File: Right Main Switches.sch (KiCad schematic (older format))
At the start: 96 parts

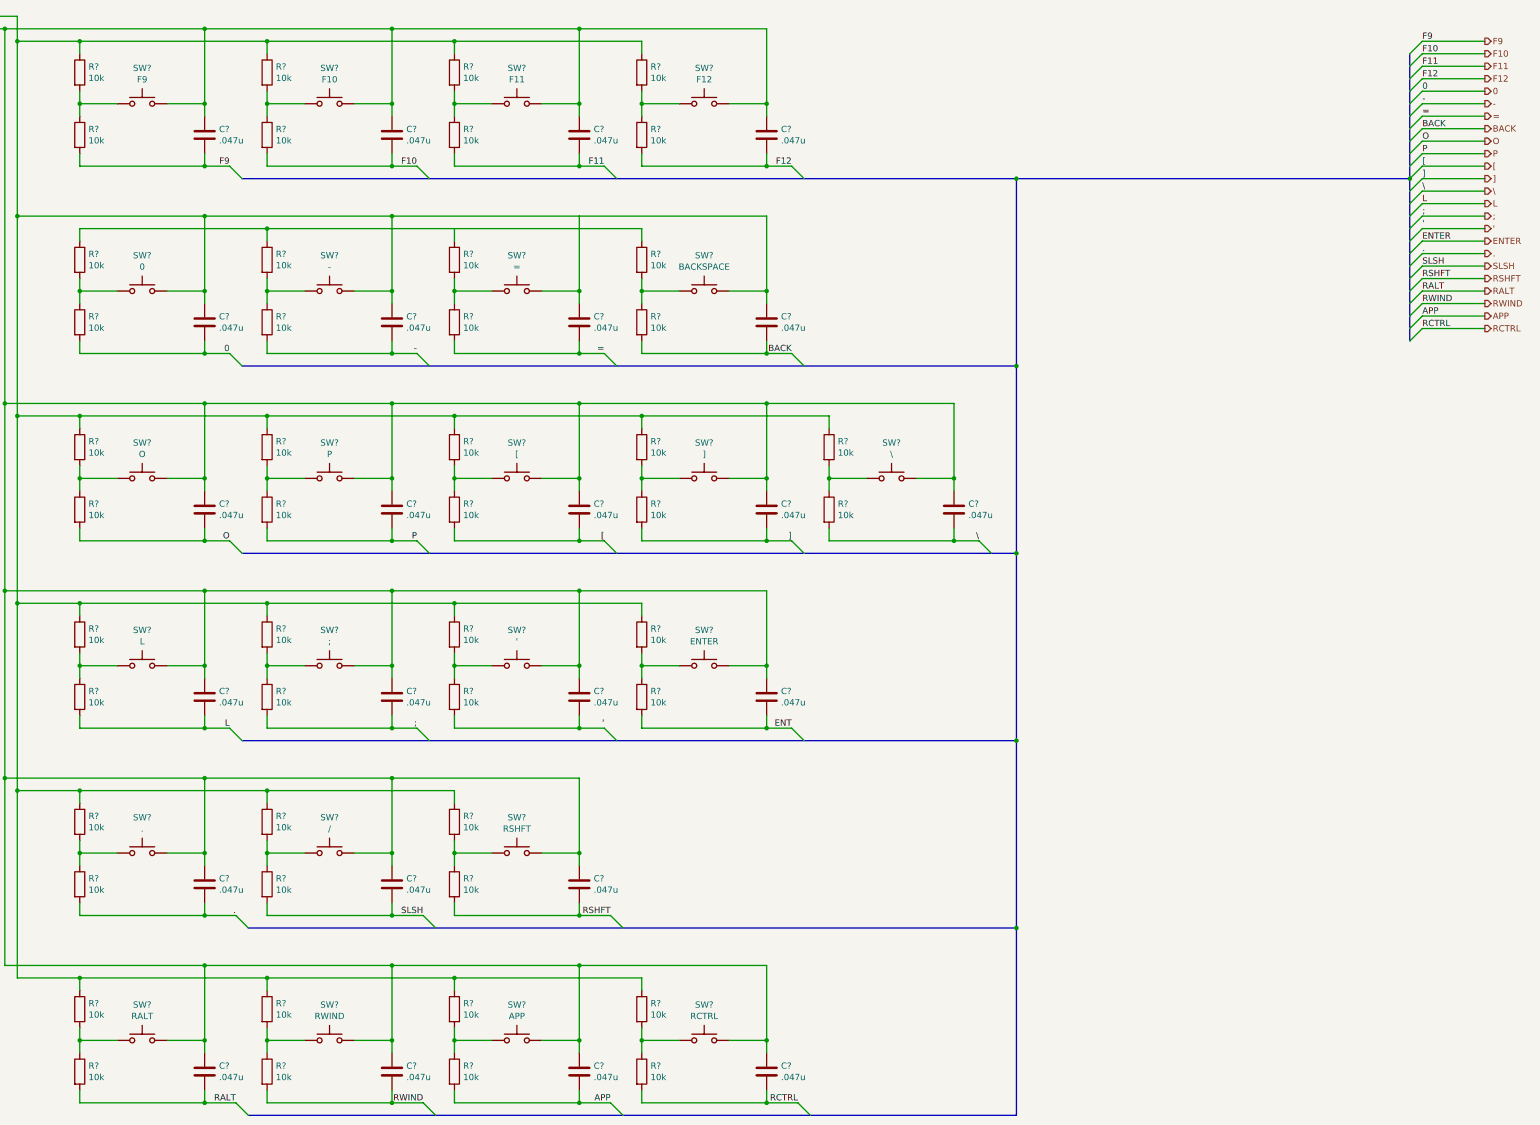
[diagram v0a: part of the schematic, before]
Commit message: Corrected errors found in design rule check
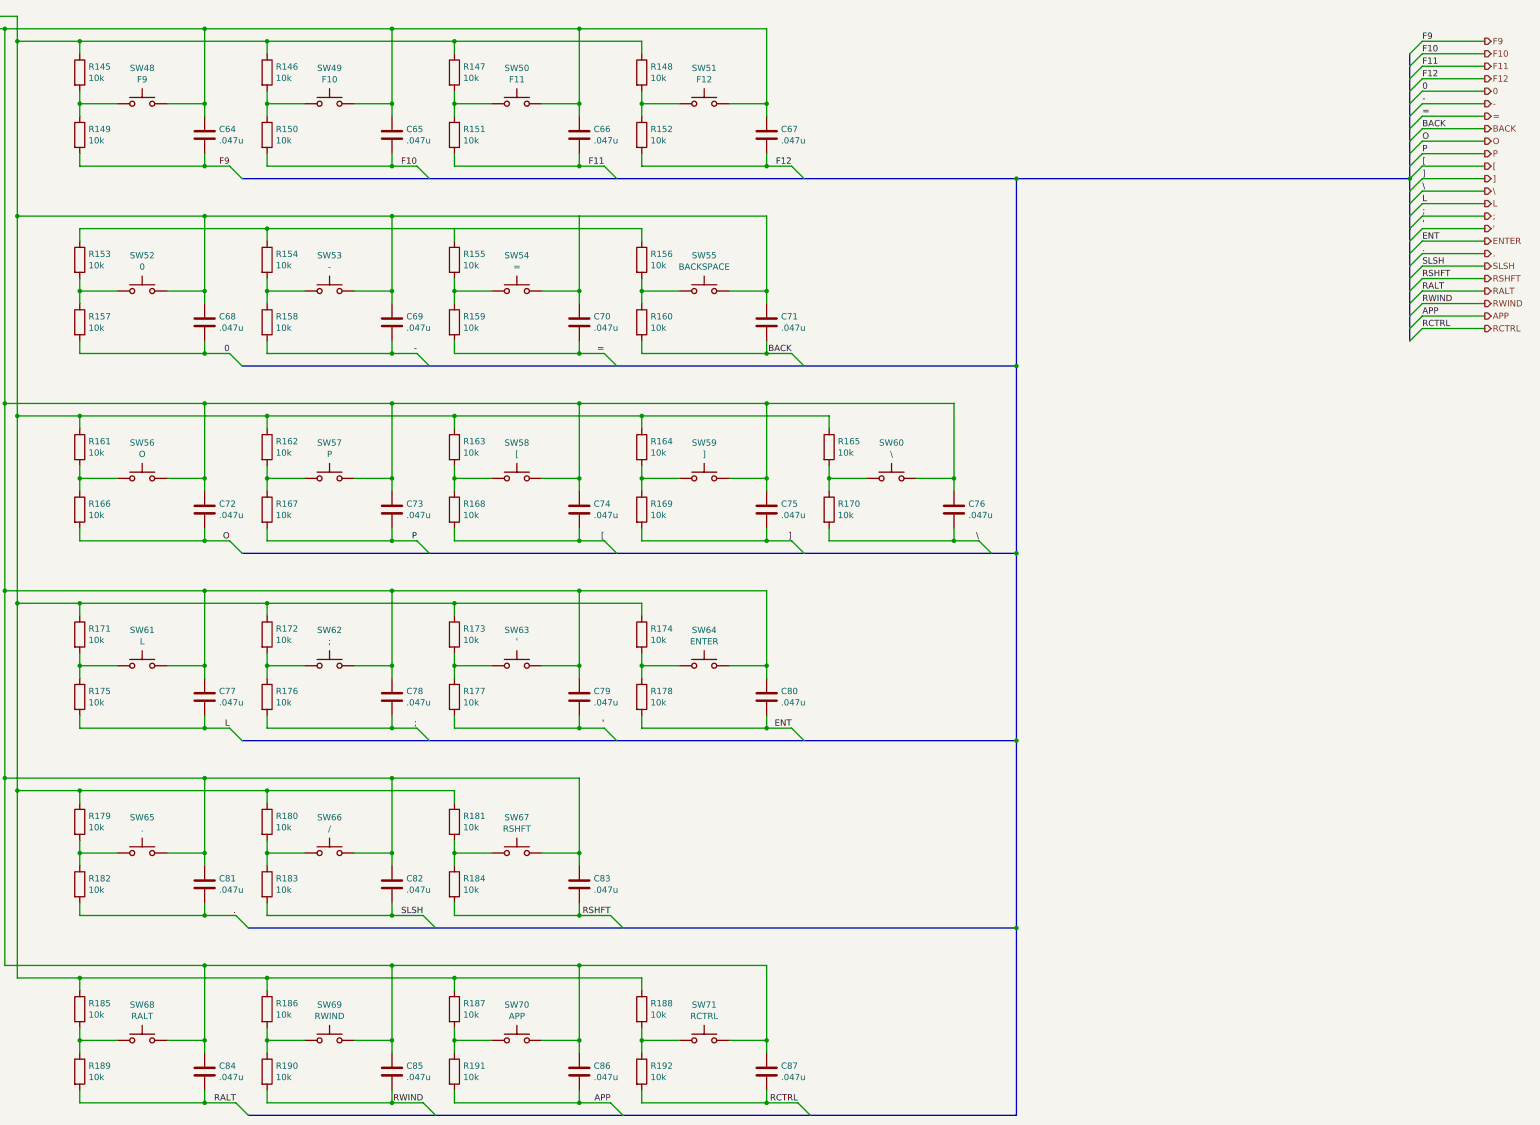
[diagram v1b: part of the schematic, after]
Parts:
- C64, C65, C66, C67, C68, C69, C70, C71, C72, C73, C74, C75, C76, C77, C78, C79, C80, C81, C82, C83, C84, C85, C86, C87: renamed from C?; footprint (none) -> Capacitor_SMD:C_1206_3216Metric_Pad1.42x1.75mm_HandSolder
- R145, R146, R147, R148, R149, R150, R151, R152, R153, R154, R155, R156, R157, R158, R159, R160, R161, R162, R163, R164, R165, R166, R167, R168, R169, R170, R171, R172, R173, R174, R175, R176, R177, R178, R179, R180, R181, R182, R183, R184, R185, R186, R187, R188, R189, R190, R191, R192: renamed from R?; footprint (none) -> Resistor_SMD:R_1206_3216Metric_Pad1.42x1.75mm_HandSolder
- SW48, SW49, SW50, SW51, SW52, SW53, SW54, SW55, SW56, SW57, SW58, SW59, SW60, SW61, SW62, SW63, SW64, SW65, SW66, SW67, SW68, SW69, SW70, SW71: renamed from SW?; footprint (none) -> Button_Switch_Keyboard:SW_Cherry_MX_1.00u_PCB
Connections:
- net ENT is gone; now on net ENTER: C80.2, R178.2

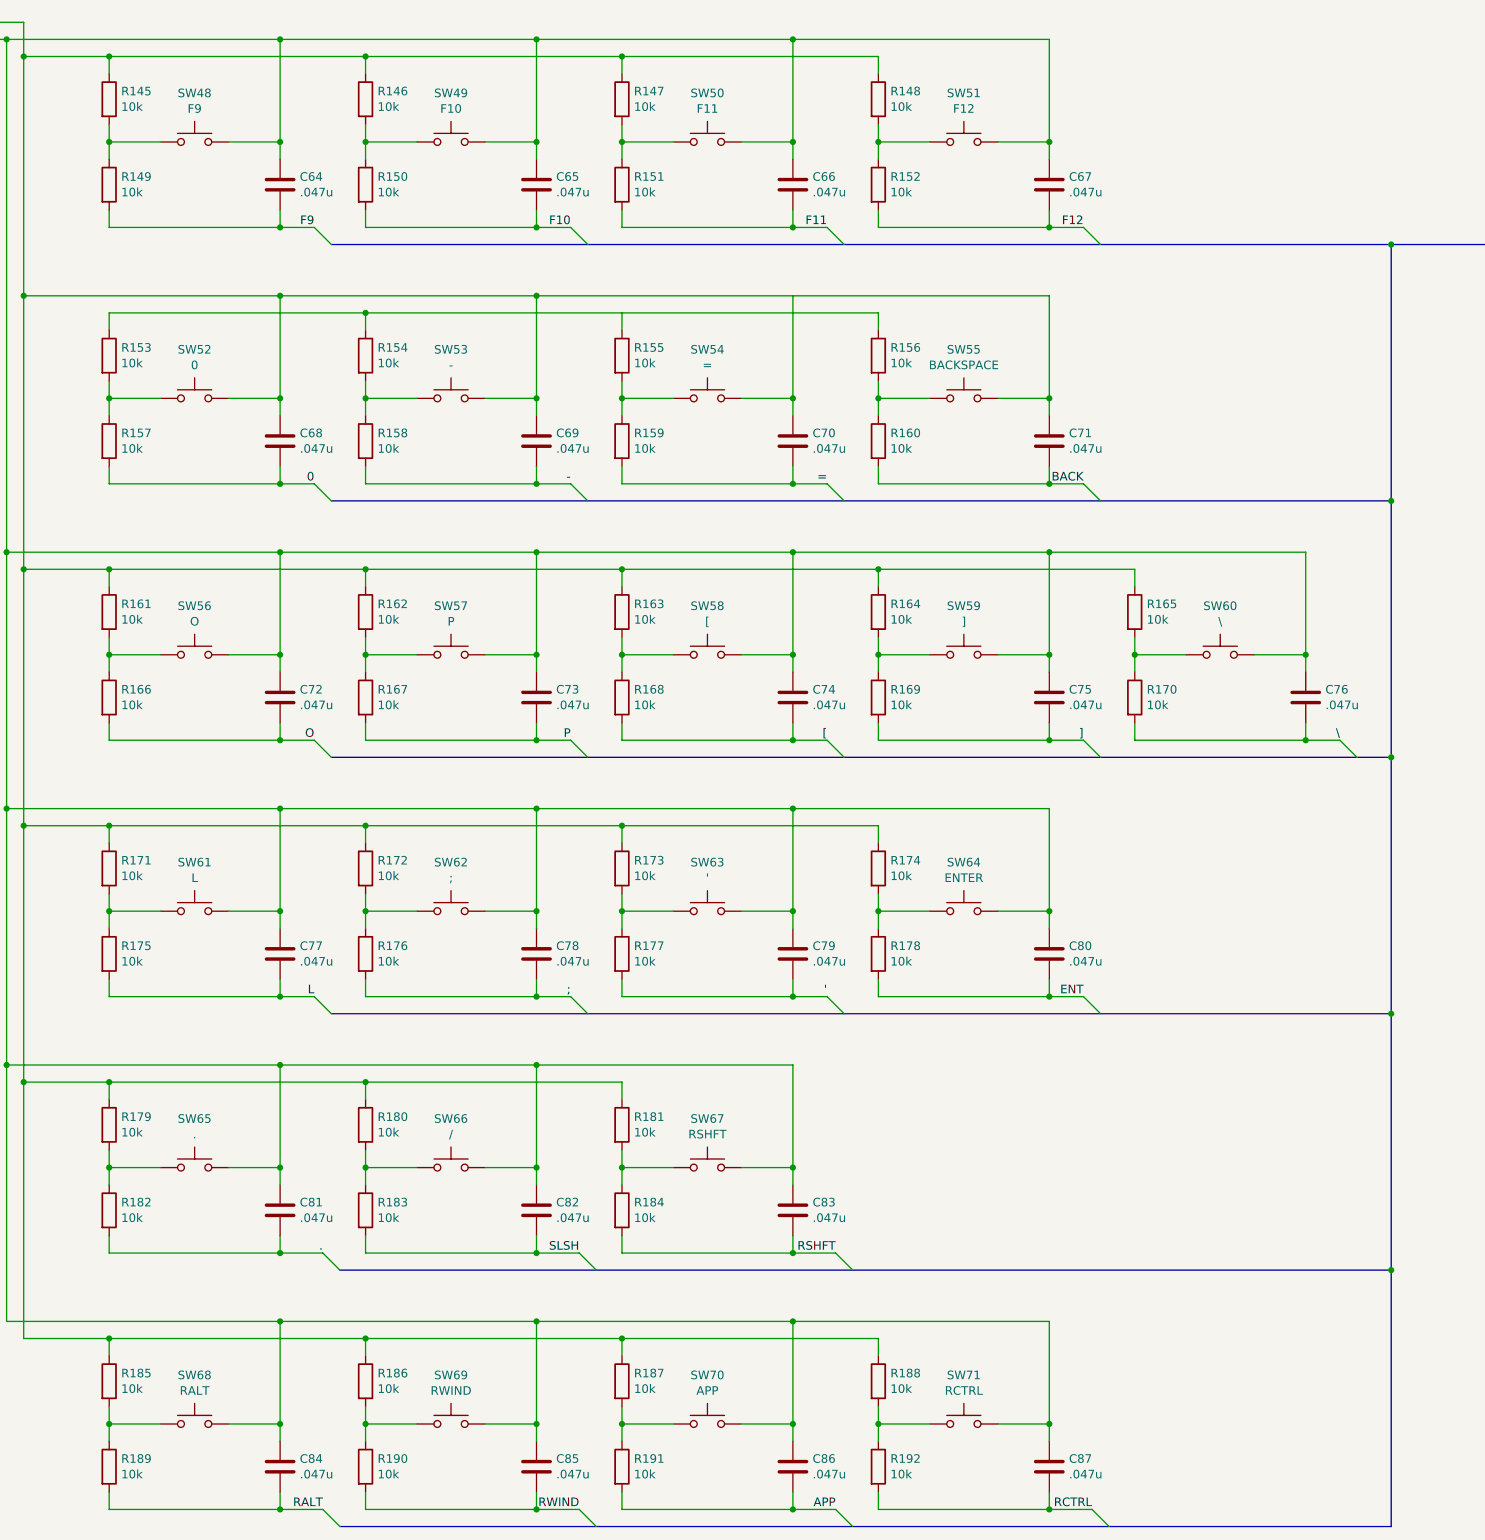
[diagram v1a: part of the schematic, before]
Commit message: Redesigned for single large PCB
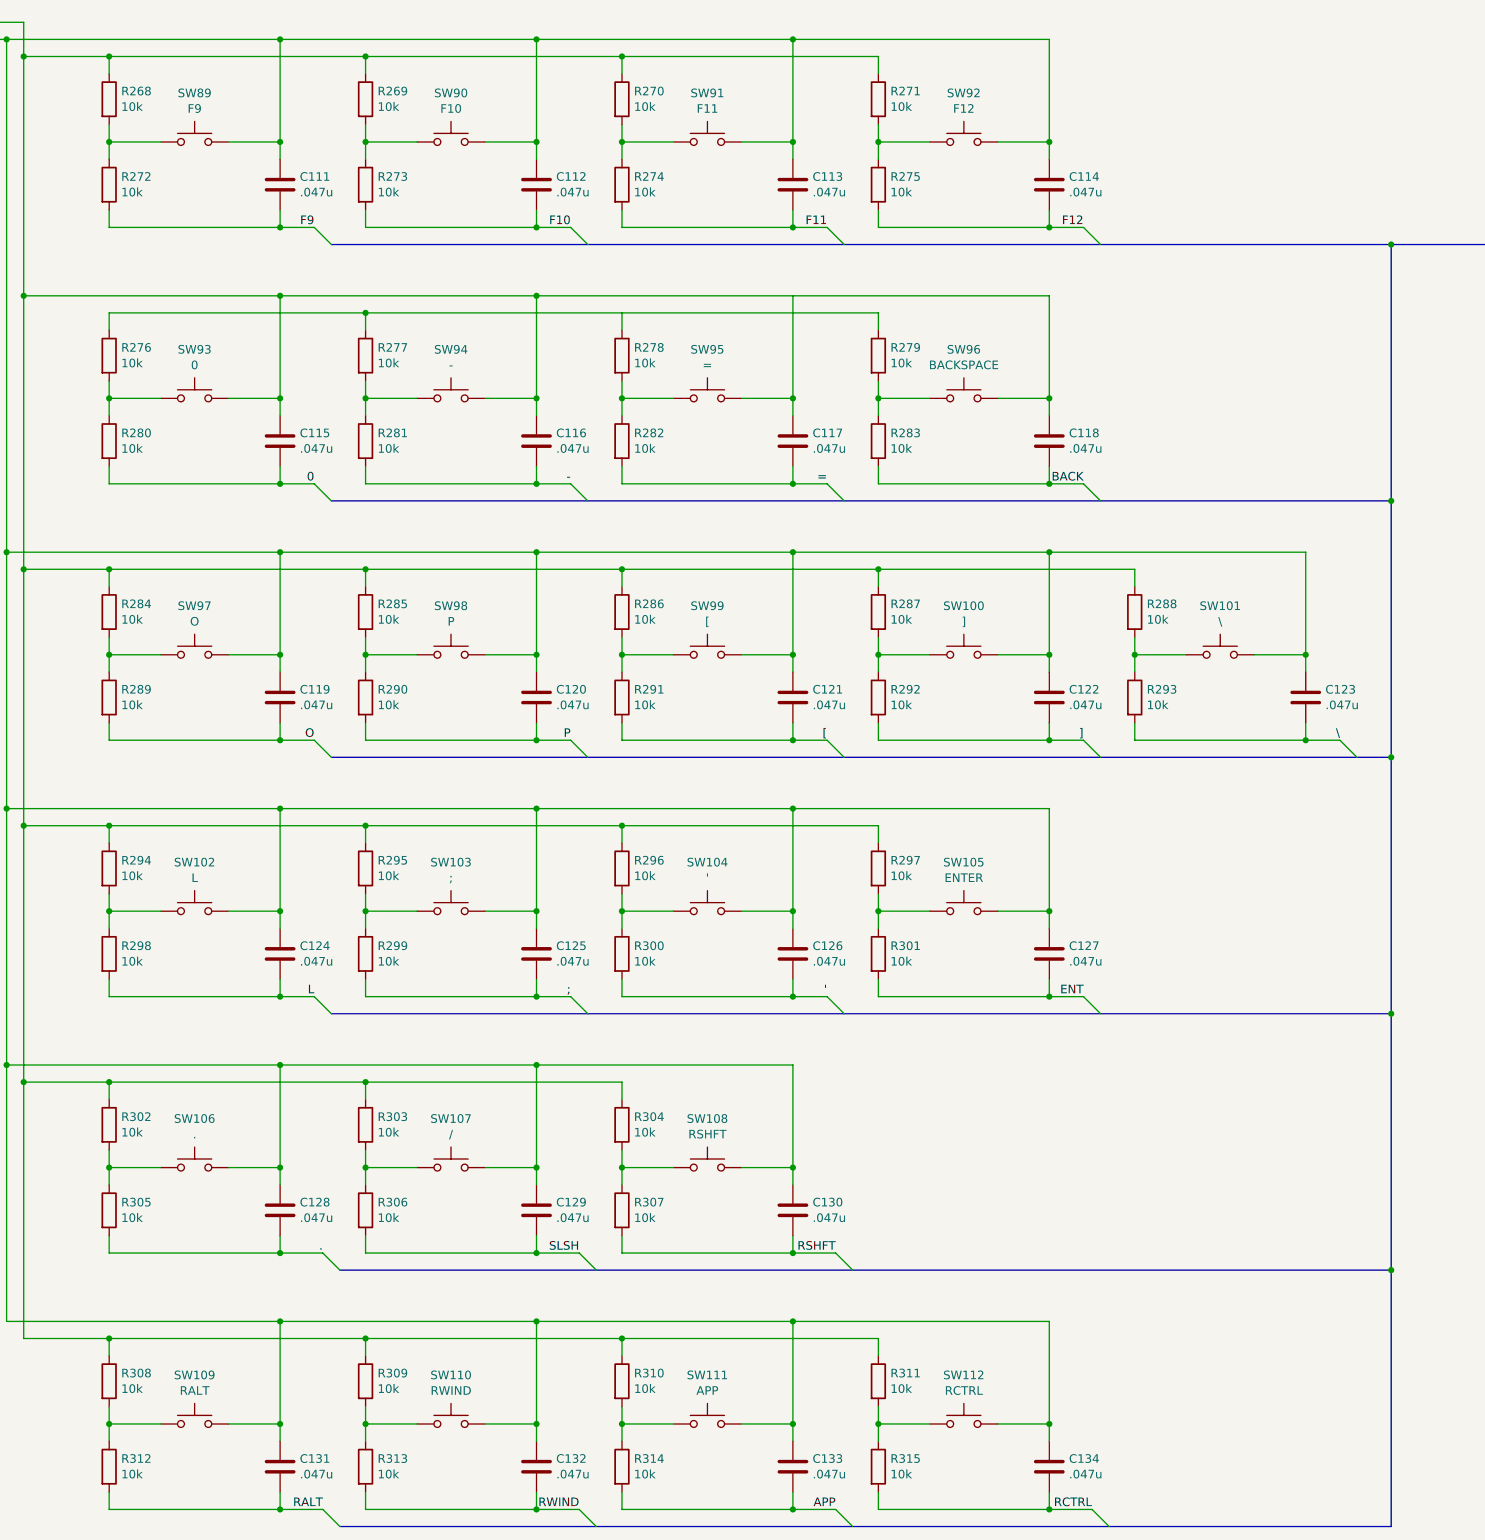
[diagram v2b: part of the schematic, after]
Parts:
- renumbered C64 to C111, C65 to C112, C66 to C113, C67 to C114, C68 to C115, C69 to C116, C70 to C117, C71 to C118, C72 to C119, C73 to C120, C74 to C121, C75 to C122, C76 to C123, C77 to C124, C78 to C125, C79 to C126, C80 to C127, C81 to C128, C82 to C129, C83 to C130, C84 to C131, C85 to C132, C86 to C133, C87 to C134, R145 to R268, R146 to R269, R147 to R270, R148 to R271, R149 to R272, R150 to R273, R151 to R274, R152 to R275, R153 to R276, R154 to R277, R155 to R278, R156 to R279, R157 to R280, R158 to R281, R159 to R282, R160 to R283, R161 to R284, R162 to R285, R163 to R286, R164 to R287, R165 to R288, R166 to R289, R167 to R290, R168 to R291, R169 to R292, R170 to R293, R171 to R294, R172 to R295, R173 to R296, R174 to R297, R175 to R298, R176 to R299, R177 to R300, R178 to R301, R179 to R302, R180 to R303, R181 to R304, R182 to R305, R183 to R306, R184 to R307, R185 to R308, R186 to R309, R187 to R310, R188 to R311, R189 to R312, R190 to R313, R191 to R314, R192 to R315, SW59 to SW100, SW60 to SW101, SW61 to SW102, SW62 to SW103, SW63 to SW104, SW64 to SW105, SW65 to SW106, SW66 to SW107, SW67 to SW108, SW68 to SW109, SW69 to SW110, SW70 to SW111, SW71 to SW112, SW48 to SW89, SW49 to SW90, SW50 to SW91, SW51 to SW92, SW52 to SW93, SW53 to SW94, SW54 to SW95, SW55 to SW96, SW56 to SW97, SW57 to SW98, SW58 to SW99

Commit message: PCB Routed, minor circuit changes
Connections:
- net 3.3V: now also R276.1, R277.1, R278.1, R279.1; no longer C115.1, C116.1, C117.1, C118.1, SW93.2, SW94.2, SW95.2, SW96.2
- net GND: now also C115.1, C116.1, C117.1, C118.1, SW93.2, SW94.2, SW95.2, SW96.2
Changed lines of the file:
@@
 $Descr B 17000 11000
 encoding utf-8
-Sheet 11 14
+Sheet 13 14
 Title ""
 Date ""
@@
 Connection ~ 8400 8200
 Wire Wire Line
-	3900 1200 3900 2600
-Wire Wire Line
-	3800 1100 3800 4100
-Wire Wire Line
 	3900 1200 4400 1200
 $Comp
@@
 	5400 1700 5400 1800
 Connection ~ 4400 1200
-Wire Wire Line
-	5400 2600 3900 2600
 Text Label 5600 2200 2    50   ~ 0
 F9
@@
 Connection ~ 3800 1100
 Connection ~ 5400 1100
-Connection ~ 3900 2600
-Wire Wire Line
-	3900 2600 3900 4200
-Connection ~ 5400 2600
 Wire Bus Line
 	11900 2300 11900 3800
@@
 RCTRL
 Connection ~ 15050 2300
+$Comp
+L Device:C C?
+U 1 1 5F59E0C0
+P 9900 4950
+AR Path="/5E8C7194/5E975AF9/5F59E0C0" Ref="C?"  Part="1"
+AR Path="/5E8C755A/5E9908F6/5F59E0C0" Ref="C?"  Part="1"
+AR Path="/5E8C755A/5EAE0F3A/5F59E0C0" Ref="C?"  Part="1"
+AR Path="/5E8C8F52/5E95E7A2/5F59E0C0" Ref="C?"  Part="1"
+AR Path="/5E8C77AE/5F496AF7/5F59E0C0" Ref="C?"  Part="1"
+AR Path="/5E8C77AE/5F4A8DAD/5F59E0C0" Ref="C?"  Part="1"
+AR Path="/5E8C79BD/6064AD62/5F59E0C0" Ref="C?"  Part="1"
+AR Path="/5E8C7194/5ED01708/5F59E0C0" Ref="C122"  Part="1"
+F 0 "C122" H 10015 4996 50  0000 L CNN
+F 1 ".047u" H 10015 4905 50  0000 L CNN
+F 2 "Capacitor_SMD:C_1206_3216Metric_Pad1.42x1.75mm_HandSolder" H 9938 4800 50  0001 C CNN
+F 3 "~" H 9900 4950 50  0001 C CNN
+	1    9900 4950
+	1    0    0    -1
+$EndComp
+Wire Wire Line
+	3800 1100 3800 2600
+Wire Wire Line
+	3900 1200 3900 2700
+Wire Wire Line
+	5400 2600 3800 2600
+Connection ~ 5400 2600
+Connection ~ 3800 2600
+Wire Wire Line
+	3800 2600 3800 4100
+Wire Wire Line
+	4400 2700 3900 2700
 Wire Bus Line
 	5750 8300 11900 8300
@@
 Wire Bus Line
 	15050 2300 15050 3600
-$Comp
-L Device:C C?
-U 1 1 5F59E0C0
-P 9900 4950
-AR Path="/5E8C7194/5E975AF9/5F59E0C0" Ref="C?"  Part="1"
-AR Path="/5E8C755A/5E9908F6/5F59E0C0" Ref="C?"  Part="1"
-AR Path="/5E8C755A/5EAE0F3A/5F59E0C0" Ref="C?"  Part="1"
-AR Path="/5E8C8F52/5E95E7A2/5F59E0C0" Ref="C?"  Part="1"
-AR Path="/5E8C77AE/5F496AF7/5F59E0C0" Ref="C?"  Part="1"
-AR Path="/5E8C77AE/5F4A8DAD/5F59E0C0" Ref="C?"  Part="1"
-AR Path="/5E8C79BD/6064AD62/5F59E0C0" Ref="C?"  Part="1"
-AR Path="/5E8C7194/5ED01708/5F59E0C0" Ref="C122"  Part="1"
-F 0 "C122" H 10015 4996 50  0000 L CNN
-F 1 ".047u" H 10015 4905 50  0000 L CNN
-F 2 "Capacitor_SMD:C_1206_3216Metric_Pad1.42x1.75mm_HandSolder" H 9938 4800 50  0001 C CNN
-F 3 "~" H 9900 4950 50  0001 C CNN
-	1    9900 4950
-	1    0    0    -1
-$EndComp
+Connection ~ 4400 2700
+Connection ~ 3900 2700
+Wire Wire Line
+	3900 2700 3900 4200
 $EndSCHEMATC
